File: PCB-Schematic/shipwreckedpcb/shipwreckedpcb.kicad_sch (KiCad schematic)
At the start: 135 parts, among them J1 USB4105, J2 Waveshare 1.54" E-Ink, Q1 Si1308EDL, SW1 BOOTSEL, SW10 Capacitive, SW11 Clicky - THT, SW12 Clicky - SMD, SW13 Clicky - THT, SW14 Clicky - SMD, SW15 Clicky - THT, SW16 Clicky - SMD, SW17 Clicky - THT, SW18 Clicky - SMD, SW2 RESET, SW3 Capacitive, SW4 Capacitive, SW5 Capacitive, SW6 Capacitive, SW7 Capacitive, SW8 Capacitive, SW9 Capacitive, U1 RP2040, U2 W25Q128JVS, U3 Si4463, U4 TPS61200DRC, U5 AS179-92LF, Y1 ABM8-272-T3, Y2 30MHz

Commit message: finished first version of schematic
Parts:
- added C56, C57: 100nF, symbol Device:C_Small
- added J3, J4: GPIO, symbol Connector_Generic:Conn_01x18
- added J5: SWD, symbol Connector_Generic:Conn_01x03
- added JP1: A0, symbol Jumper:Jumper_2_Open
- added JP2: A1, symbol Jumper:Jumper_2_Open
- added JP3: A2, symbol Jumper:Jumper_2_Open
- added L10: NFC Antenna, symbol Device:L_Small
- added R20, R21, R22: 10k, symbol Device:R_Small_US
- added SW19: PWR Switch, symbol Switch:SW_SPDT
- added U7: PCA9555PW, Package_SO:TSSOP-24_4.4x7.8mm_P0.65mm, symbol Interface_Expansion:PCA9555PW
- added U8: ST25DV04K-IE6S3, Package_SO:SO-8_3.9x4.9mm_P1.27mm, symbol RF_NFC:ST25DV04K-IER8C3
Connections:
- net +3V3: now also C56.1, C57.1, J3.2 (Pin_2), J4.10 (Pin_10), J4.11 (Pin_11), J4.12 (Pin_12), J4.13 (Pin_13), J4.14 (Pin_14), J4.15 (Pin_15), J4.16 (Pin_16), J4.17 (Pin_17), JP1.1 (A), JP2.1 (A), JP3.1 (A), U7.24 (VDD), U8.8 (VCC)
- net +BATT: now also SW19.1 (A); no longer BT1.1 (+), C51.2
- net Earth: now also C56.2, C57.2, J3.1 (Pin_1), J3.13 (Pin_13), J3.18 (Pin_18), J3.7 (Pin_7), J4.1 (Pin_1), J4.18 (Pin_18), J4.3 (Pin_3), J4.6 (Pin_6), J4.9 (Pin_9), J5.2 (Pin_2), R20.2, R21.2, R22.2, U7.12 (VSS), U8.4 (VSS)
- net GPIO10: now also J3.10 (Pin_10); no longer SW13.2
- net GPIO11: now also J3.11 (Pin_11); no longer SW14.2
- net GPIO12: now also J3.12 (Pin_12); no longer SW15.2
- net GPIO13: now also J3.14 (Pin_14); no longer SW16.2
- net GPIO14: now also J3.15 (Pin_15); no longer SW17.2
- net GPIO15: now also J3.16 (Pin_16); no longer SW18.2
- net GPIO29_ADC3: now also J3.17 (Pin_17)
- net GPIO4: now also J3.3 (Pin_3); no longer R14.2, SW7.2
- net GPIO5: now also J3.4 (Pin_4); no longer R15.2, SW8.2
- net GPIO6: now also J3.5 (Pin_5); no longer R16.2, SW9.2
- net GPIO7: now also J3.6 (Pin_6); no longer R17.2, SW10.2
- net GPIO8: now also J3.8 (Pin_8); no longer SW11.2
- net GPIO9: now also J3.9 (Pin_9); no longer SW12.2
- net SPI_CLK: now also J4.2 (Pin_2)
- net SPI_MISO: now also J4.5 (Pin_5)
- net SPI_MOSI: now also J4.4 (Pin_4)
- net RP_SWCLK: now reaches U1.24 (SWCLK)
- net RP_SWCLK: now also J5.1 (Pin_1)
- net RP_SWDIO: now reaches U1.25 (SWD)
- net RP_SWDIO: now also J5.3 (Pin_3)
- net GPIO0 renamed BUTT_1
- net BUTT_1: now also U7.4 (IO0_0); no longer U1.2 (GPIO0)
- net GPIO1 renamed BUTT_2
- net BUTT_2: now also U7.5 (IO0_1); no longer U1.3 (GPIO1)
- net GPIO2 renamed BUTT_3
- net BUTT_3: now also U7.6 (IO0_2); no longer U1.4 (GPIO2)
- net GPIO3 renamed BUTT_4
- net BUTT_4: now also U7.7 (IO0_3); no longer U1.5 (GPIO3)
- new net: L10.1, U8.2 (AC0)
- new net: L10.2, U8.3 (AC1)
- new net BT Power: BT1.1 (+), C51.2, SW19.2 (B)
- new net BUTT_10: SW12.2, U7.14 (IO1_1)
- new net BUTT_11: SW13.2, U7.15 (IO1_2)
- new net BUTT_12: SW14.2, U7.16 (IO1_3)
- new net BUTT_13: SW15.2, U7.17 (IO1_4)
- new net BUTT_14: SW16.2, U7.18 (IO1_5)
- new net BUTT_15: SW17.2, U7.19 (IO1_6)
- new net BUTT_16: SW18.2, U7.20 (IO1_7)
- new net BUTT_5: R14.2, SW7.2, U7.8 (IO0_4)
- new net BUTT_6: R15.2, SW8.2, U7.9 (IO0_5)
- new net BUTT_7: R16.2, SW9.2, U7.10 (IO0_6)
- new net BUTT_8: R17.2, SW10.2, U7.11 (IO0_7)
- new net BUTT_9: SW11.2, U7.13 (IO1_0)
- new net I2C_SCL: J4.8 (Pin_8), U1.3 (GPIO1), U7.22 (SCL), U8.6 (SCL)
- new net I2C_SDA: J4.7 (Pin_7), U1.2 (GPIO0), U7.23 (SDA), U8.5 (SDA)
- new net IO_A0: JP1.2 (B), R20.1, U7.21 (A0)
- new net IO_A1: JP2.2 (B), R21.1, U7.2 (A1)
- new net IO_A2: JP3.2 (B), R22.1, U7.3 (A2)
- new net IO_INT: U1.4 (GPIO2), U7.1 (~{INT})
- new net NFC_GPO: U1.5 (GPIO3), U8.7 (GPO)
- no-connect marks 10 -> 13
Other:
- note added: "IO Expander"
- note added: "Need to find a way to add more GPIO"
- moved on the sheet: BZ1, C12, C24, U3, Y2

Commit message: add footprints for everything (just gotta sort out the touch pads)
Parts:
- removed L10: NFC Antenna, symbol Device:L_Small
- removed Y2: 30MHz, symbol Device:Crystal
- added C58, C59: 12pF, Capacitor_SMD:C_0603_1608Metric, symbol Device:C_Small
- added D5: LED, LED_SMD:LED_0603_1608Metric, symbol Device:LED
- added R23: 47, Resistor_SMD:R_0603_1608Metric, symbol Device:R_Small_US
- added Y2: X322530MOB4SI, Crystal:Crystal_SMD_3225-4Pin_3.2x2.5mm, symbol Device:Crystal_GND24
- AE1: footprint (none) -> Connector_PinSocket_2.54mm:PinSocket_1x01_P2.54mm_Vertical
- BT1: footprint (none) -> Battery:BatteryHolder_Keystone_2462_2xAA
- BZ1: footprint (none) -> Connector_PinSocket_2.54mm:PinSocket_1x02_P2.54mm_Vertical
- C1, C10, C11, C12, C13, C14, C15, C16, C17, C18, C19, C2, C20, C21, C22, C23, C24, C25, C26, C27, C28, C29, C3, C30, C31, C32, C33, C34, C35, C36, C37, C38, C39, C4, C40, C5, C51, C52, C53, C54, C55, C56, C57, C6, C7, C8, C9: footprint (none) -> Capacitor_SMD:C_0603_1608Metric
- C41, C42, C43, C44, C45, C46, C47, C48, C49, C50: footprint (none) -> Capacitor_SMD:C_0402_1005Metric
- D1: footprint (none) -> LED_SMD:LED_0603_1608Metric
- D2, D3, D4: footprint (none) -> Diode_SMD:D_SOD-123
- FB1, R1, R10, R11, R12, R13, R14, R15, R16, R17, R18, R19, R2, R20, R21, R22, R3, R4, R5, R6, R7, R8, R9: footprint (none) -> Resistor_SMD:R_0603_1608Metric
- J3, J4: footprint (none) -> Connector_PinSocket_2.54mm:PinSocket_1x18_P2.54mm_Vertical
- J5: footprint (none) -> Connector_PinSocket_2.54mm:PinSocket_1x03_P2.54mm_Vertical
- JP1, JP2, JP3: footprint (none) -> Jumper:SolderJumper-2_P1.3mm_Open_RoundedPad1.0x1.5mm
- L1: footprint (none) -> Inductor_SMD:L_0603_1608Metric
- L2, L3, L4, L5, L6, L7, L8: footprint (none) -> Inductor_SMD:L_0402_1005Metric
- L9: footprint (none) -> Inductor_SMD:L_Taiyo-Yuden_NR-30xx
- SW1, SW12, SW14, SW16, SW18, SW2: footprint (none) -> Button_Switch_SMD:SW_Tactile_SPST_NO_Straight_CK_PTS636Sx25SMTRLFS
- SW10, SW3, SW4, SW5, SW6, SW7, SW8, SW9: value Capacitive -> Resistive
- SW11, SW13, SW15, SW17: footprint (none) -> Button_Switch_THT:SW_PUSH_6mm
- SW19: footprint (none) -> Button_Switch_SMD:SW_SPDT_PCM12
- Y1: footprint (none) -> Crystal:Crystal_SMD_Abracon_ABM8G-4Pin_3.2x2.5mm
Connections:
- net Earth: now also C58.1, C59.1, D5.1 (K), Y2.2, Y2.4
- net at U8.1 (V_EH): now also R23.1
- net at U8.2 (AC0): now also U8.3 (AC1)
- net SI_XOUT: now reaches U3.16 (XOUT)
- net SI_XOUT: now also C59.2, Y2.1
- net SI_XIN: now reaches U3.17 (XIN)
- net SI_XIN: now also C58.2, Y2.3
- new net: D5.2 (A), R23.2
- no-connect marks 13 -> 12
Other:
- note added: "NFC Antenna"
- note added: "clicky buttons: C318938 XKB Connection TS-1101-C-W - pw switch: SK-3296S-01-L1"
- moved on the sheet: C24, U3

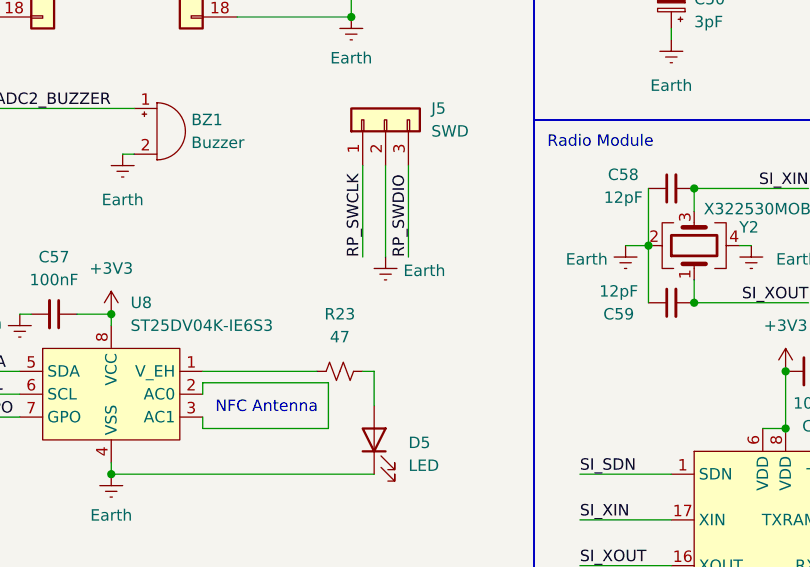
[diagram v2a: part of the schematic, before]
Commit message: finish assigning footprints, made resistive button
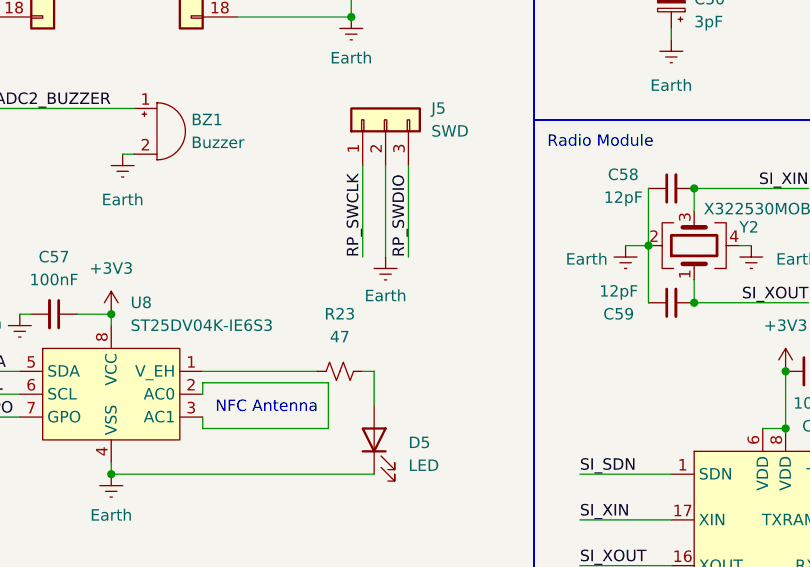
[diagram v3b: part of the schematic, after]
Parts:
- D1: footprint LED_SMD:LED_0603_1608Metric -> Diode_SMD:D_0603_1608Metric
- SW10, SW3, SW4, SW5, SW6, SW7, SW8, SW9: footprint (none) -> Resistive_Touch:Resistive_Button_130mil
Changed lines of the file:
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@@
 			)
 		)
-		(property "Footprint" ""
+		(property "Footprint" "Resistive_Touch:Resistive_Button_130mil"
 			(at 233.68 254 0)
 			(effects
@@
 		)
 		(property "Value" "Earth"
-			(at 104.648 115.824 0)
+			(at 100.33 118.618 0)
 			(effects
 				(font
@@
 			)
 		)
-		(property "Footprint" ""
+		(property "Footprint" "Resistive_Touch:Resistive_Button_130mil"
 			(at 233.68 196.85 0)
 			(effects
@@
 			)
 		)
-		(property "Footprint" ""
+		(property "Footprint" "Resistive_Touch:Resistive_Button_130mil"
 			(at 233.68 208.28 0)
 			(effects
@@
 			)
 		)
-		(property "Footprint" "LED_SMD:LED_0603_1608Metric"
+		(property "Footprint" "Diode_SMD:D_0603_1608Metric"
 			(at 200.66 123.19 0)
 			(effects
@@
 			)
 		)
-		(property "Footprint" ""
+		(property "Footprint" "Resistive_Touch:Resistive_Button_130mil"
 			(at 233.68 242.57 0)
 			(effects
@@
 			)
 		)
-		(property "Footprint" ""
+		(property "Footprint" "Resistive_Touch:Resistive_Button_130mil"
 			(at 233.68 185.42 0)
 			(effects
@@
 			)
 		)
-		(property "Footprint" ""
+		(property "Footprint" "Resistive_Touch:Resistive_Button_130mil"
 			(at 233.68 231.14 0)
 			(effects
@@
 			)
 		)
-		(property "Footprint" ""
+		(property "Footprint" "Resistive_Touch:Resistive_Button_130mil"
 			(at 233.68 265.43 0)
 			(effects
@@
 			)
 		)
-		(property "Footprint" ""
+		(property "Footprint" "Resistive_Touch:Resistive_Button_130mil"
 			(at 233.68 219.71 0)
 			(effects

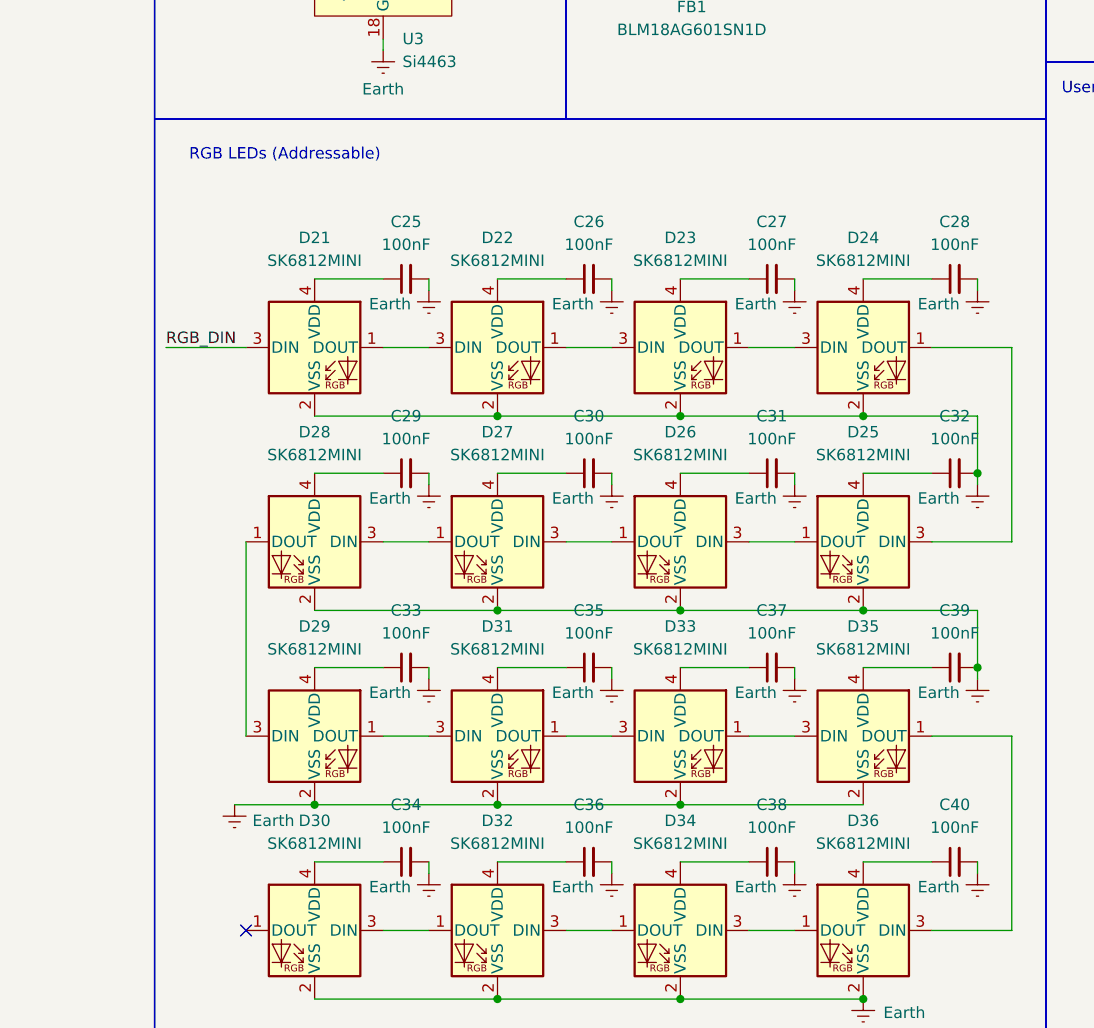
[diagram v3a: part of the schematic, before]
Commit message: add power to lights (oops), lay out individual sections, add rough placement
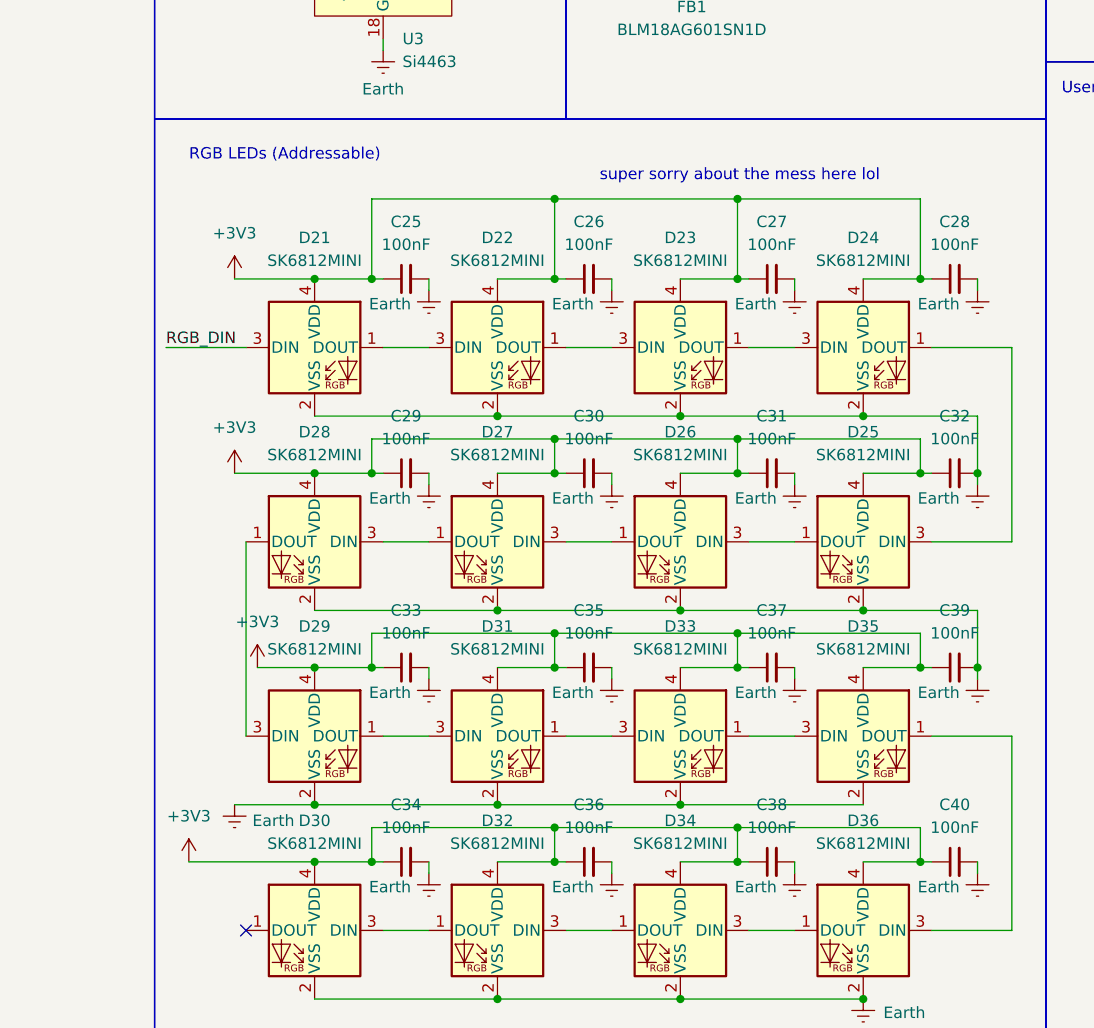
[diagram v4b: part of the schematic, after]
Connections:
- net +3V3: now also C25.1, C26.1, C27.1, C28.1, C29.1, C30.1, C31.1, C32.1, C33.1, C34.1, C35.1, C36.1, C37.1, C38.1, C39.1, C40.1, D21.4 (VDD), D22.4 (VDD), D23.4 (VDD), D24.4 (VDD), D25.4 (VDD), D26.4 (VDD), D27.4 (VDD), D28.4 (VDD), D29.4 (VDD), D30.4 (VDD), D31.4 (VDD), D32.4 (VDD), D33.4 (VDD), D34.4 (VDD), D35.4 (VDD), D36.4 (VDD)
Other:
- note added: "super sorry about the mess here lol"
